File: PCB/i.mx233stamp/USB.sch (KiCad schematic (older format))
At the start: 21 parts, among them U4 GL850G, X2 12MHz

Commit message: conectando mas senales
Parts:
- L7: footprint (none) -> SM0805
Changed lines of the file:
@@
-EESchema Schematic File Version 2  date Fri 05 Aug 2011 02:31:32 PM COT
+EESchema Schematic File Version 2  date Sat 06 Aug 2011 12:43:52 PM COT
 LIBS:con-jack
 LIBS:adm3101e
@@
 Sheet 2 4
 Title ""
-Date "5 aug 2011"
+Date "6 aug 2011"
 Rev ""
 Comp ""
@@
 $EndComp
 $Comp
-L GND #PWR12
+L GND #PWR01
 U 1 1 4E3C4430
 P 10750 3150
-F 0 "#PWR12" H 10750 3150 30  0001 C CNN
+F 0 "#PWR01" H 10750 3150 30  0001 C CNN
 F 1 "GND" H 10750 3080 30  0001 C CNN
 	1    10750 3150
@@
 $EndComp
 $Comp
-L VDD5V #PWR11
+L VDD5V #PWR02
 U 1 1 4E3C4429
 P 10750 2550
-F 0 "#PWR11" H 10750 2650 30  0001 C CNN
+F 0 "#PWR02" H 10750 2650 30  0001 C CNN
 F 1 "VDD5V" H 10750 2650 30  0000 C CNN
 	1    10750 2550
@@
 $EndComp
 $Comp
-L VDD5V #PWR7
+L VDD5V #PWR03
 U 1 1 4E3C4418
 P 9600 2550
-F 0 "#PWR7" H 9600 2650 30  0001 C CNN
+F 0 "#PWR03" H 9600 2650 30  0001 C CNN
 F 1 "VDD5V" H 9600 2650 30  0000 C CNN
 	1    9600 2550
@@
 $EndComp
 $Comp
-L GND #PWR5
+L GND #PWR04
 U 1 1 4E3C436B
 P 8500 1650
-F 0 "#PWR5" H 8500 1650 30  0001 C CNN
+F 0 "#PWR04" H 8500 1650 30  0001 C CNN
 F 1 "GND" H 8500 1580 30  0001 C CNN
 	1    8500 1650
@@
 USBH_P33V
 $Comp
-L VDD5V #PWR8
+L VDD5V #PWR05
 U 1 1 4E3C4207
 P 9600 2950
-F 0 "#PWR8" H 9600 3050 30  0001 C CNN
+F 0 "#PWR05" H 9600 3050 30  0001 C CNN
 F 1 "VDD5V" H 9600 3050 30  0000 C CNN
 	1    9600 2950
@@
 USBH_P33V
 $Comp
-L GND #PWR9
+L GND #PWR06
 U 1 1 4E3C3A60
 P 9900 5600
-F 0 "#PWR9" H 9900 5600 30  0001 C CNN
+F 0 "#PWR06" H 9900 5600 30  0001 C CNN
 F 1 "GND" H 9900 5530 30  0001 C CNN
 	1    9900 5600
@@
 $EndComp
 $Comp
-L GND #PWR4
+L GND #PWR07
 U 1 1 4E3C3A56
 P 8000 5600
-F 0 "#PWR4" H 8000 5600 30  0001 C CNN
+F 0 "#PWR07" H 8000 5600 30  0001 C CNN
 F 1 "GND" H 8000 5530 30  0001 C CNN
 	1    8000 5600
@@
 F 0 "L7" V 9150 4800 40  0000 C CNN
 F 1 "2A 120 ohm" V 9300 4800 40  0000 C CNN
+F 2 "SM0805" H 9200 4800 60  0001 C CNN
 	1    9200 4800
 	0    1    1    0
@@
 andres.calderon@emqbit.com\n
 $Comp
-L GND #PWR3
+L GND #PWR08
 U 1 1 4E3C3807
 P 7100 4300
-F 0 "#PWR3" H 7100 4300 30  0001 C CNN
+F 0 "#PWR08" H 7100 4300 30  0001 C CNN
 F 1 "GND" H 7100 4230 30  0001 C CNN
 	1    7100 4300
@@
 $EndComp
 $Comp
-L GND #PWR10
+L GND #PWR09
 U 1 1 4E3C36BE
 P 10400 3600
-F 0 "#PWR10" H 10400 3600 30  0001 C CNN
+F 0 "#PWR09" H 10400 3600 30  0001 C CNN
 F 1 "GND" H 10400 3530 30  0001 C CNN
 	1    10400 3600
@@
 X1
 $Comp
-L GND #PWR6
+L GND #PWR010
 U 1 1 4E3C222B
 P 9500 3750
-F 0 "#PWR6" H 9500 3750 30  0001 C CNN
+F 0 "#PWR010" H 9500 3750 30  0001 C CNN
 F 1 "GND" H 9500 3680 30  0001 C CNN
 	1    9500 3750
@@
 USB_DM2
 $Comp
-L GND #PWR1
+L GND #PWR011
 U 1 1 4E3C212B
 P 5250 5150
-F 0 "#PWR1" H 5250 5150 30  0001 C CNN
+F 0 "#PWR011" H 5250 5150 30  0001 C CNN
 F 1 "GND" H 5250 5080 30  0001 C CNN
 	1    5250 5150
@@
 $EndComp
 $Comp
-L GND #PWR2
+L GND #PWR012
 U 1 1 4E3C206C
 P 5850 5150
-F 0 "#PWR2" H 5850 5150 30  0001 C CNN
+F 0 "#PWR012" H 5850 5150 30  0001 C CNN
 F 1 "GND" H 5850 5080 30  0001 C CNN
 	1    5850 5150

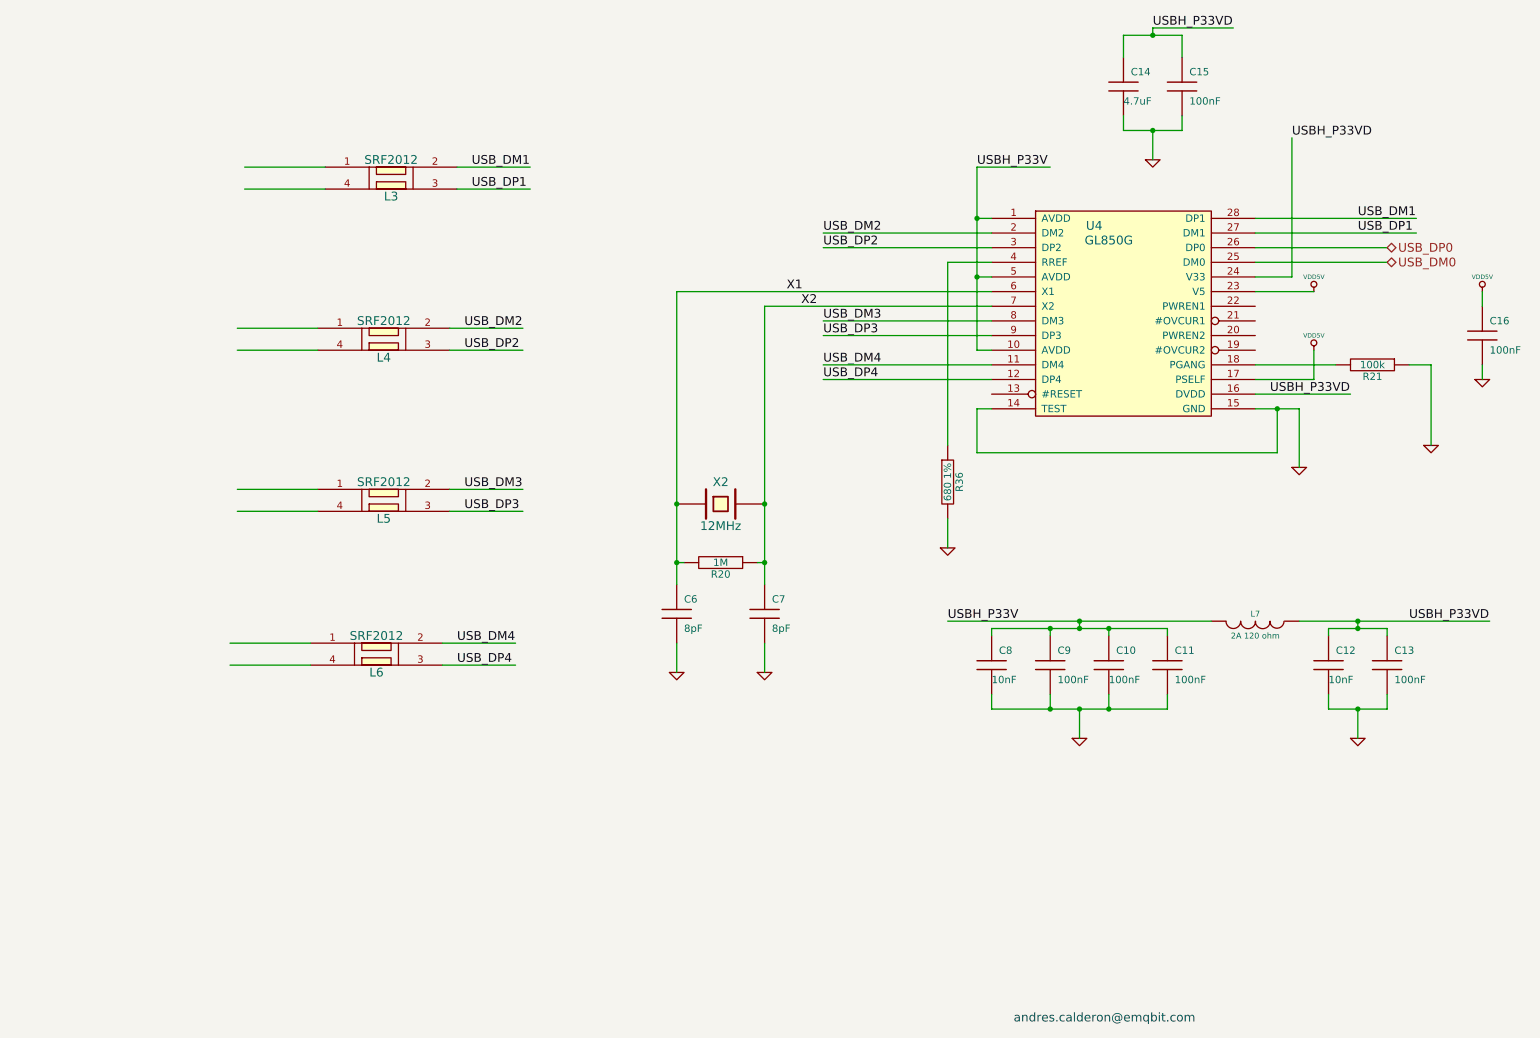
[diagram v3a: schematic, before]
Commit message: Cambios en los footprints, adición de conectores USB host, organización de señales en los conectores
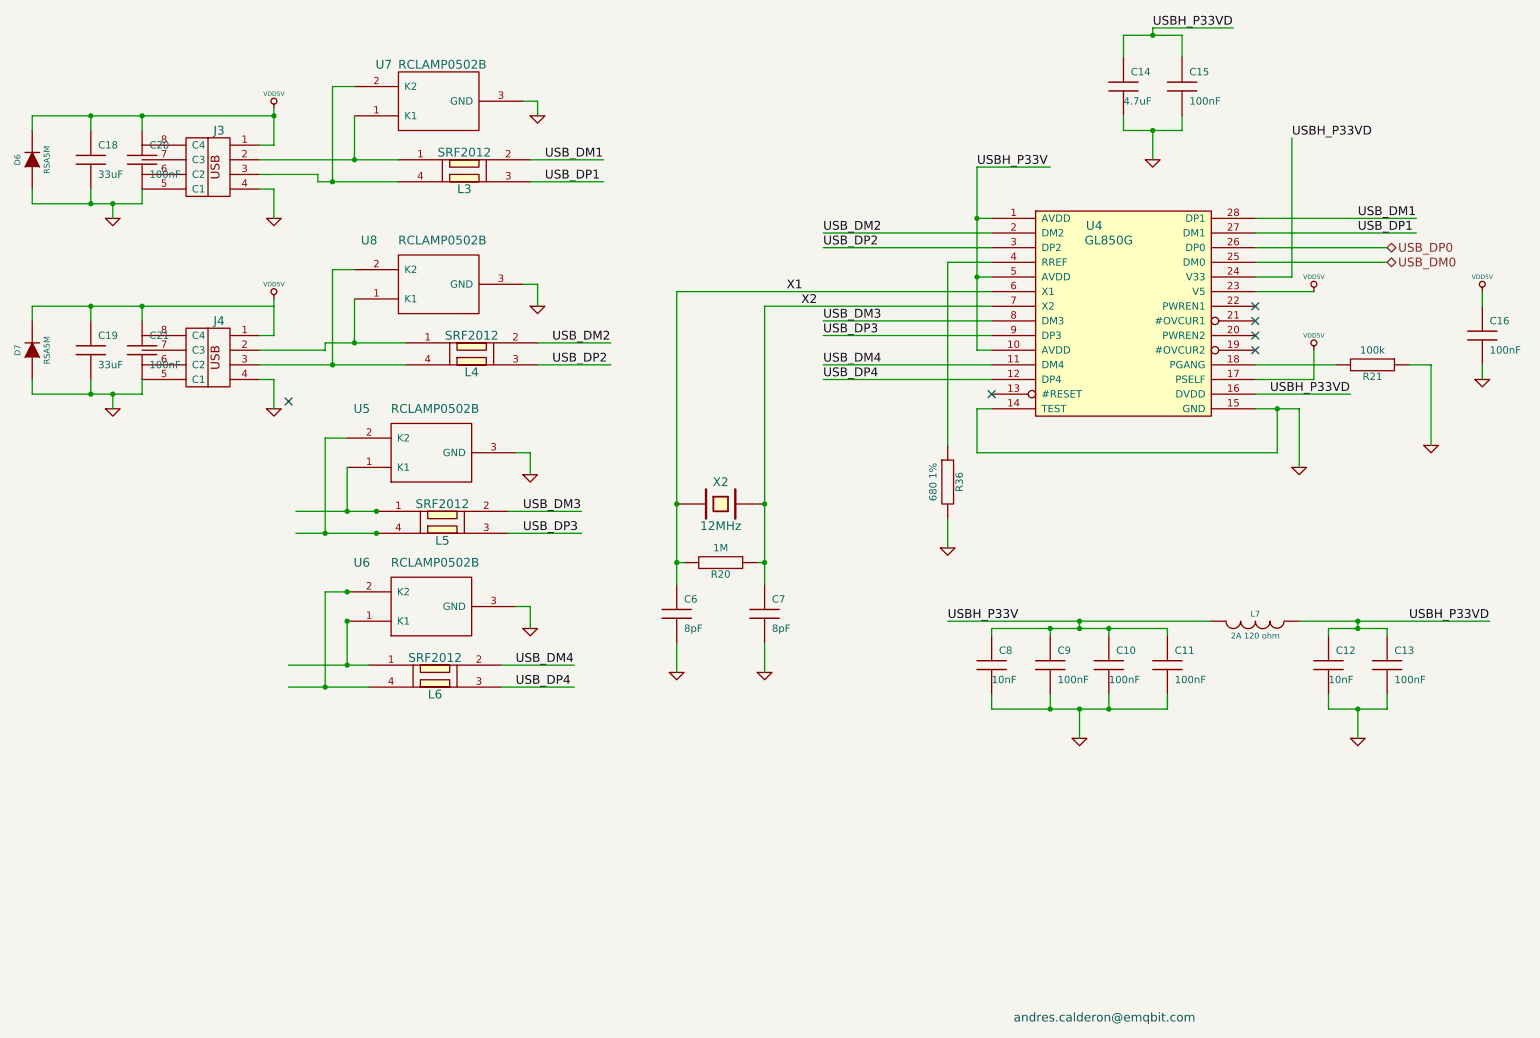
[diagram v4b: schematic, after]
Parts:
- added C18, C19: 33uF, SM1206, symbol C
- added C20, C21: 100nF, SM0603, symbol C
- added D6, D7: RSA5M, diode-1-SOD123, symbol DIODE
- added J3, J4: USB_2, conn_usb_A-vert, symbol USB_2
- added U5, U6, U7, U8: RCLAMP0502B, SOD523, symbol RCLAMP0502B
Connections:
- wire segments 90 -> 140
- no-connect marks 0 -> 6
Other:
- moved on the sheet: L3, L4, L5, L6

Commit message: Adición de conectores USB host, conexión de HP_GND a un conector externo, Cambio de los footprints dela DDR memoria SPI, Q1,
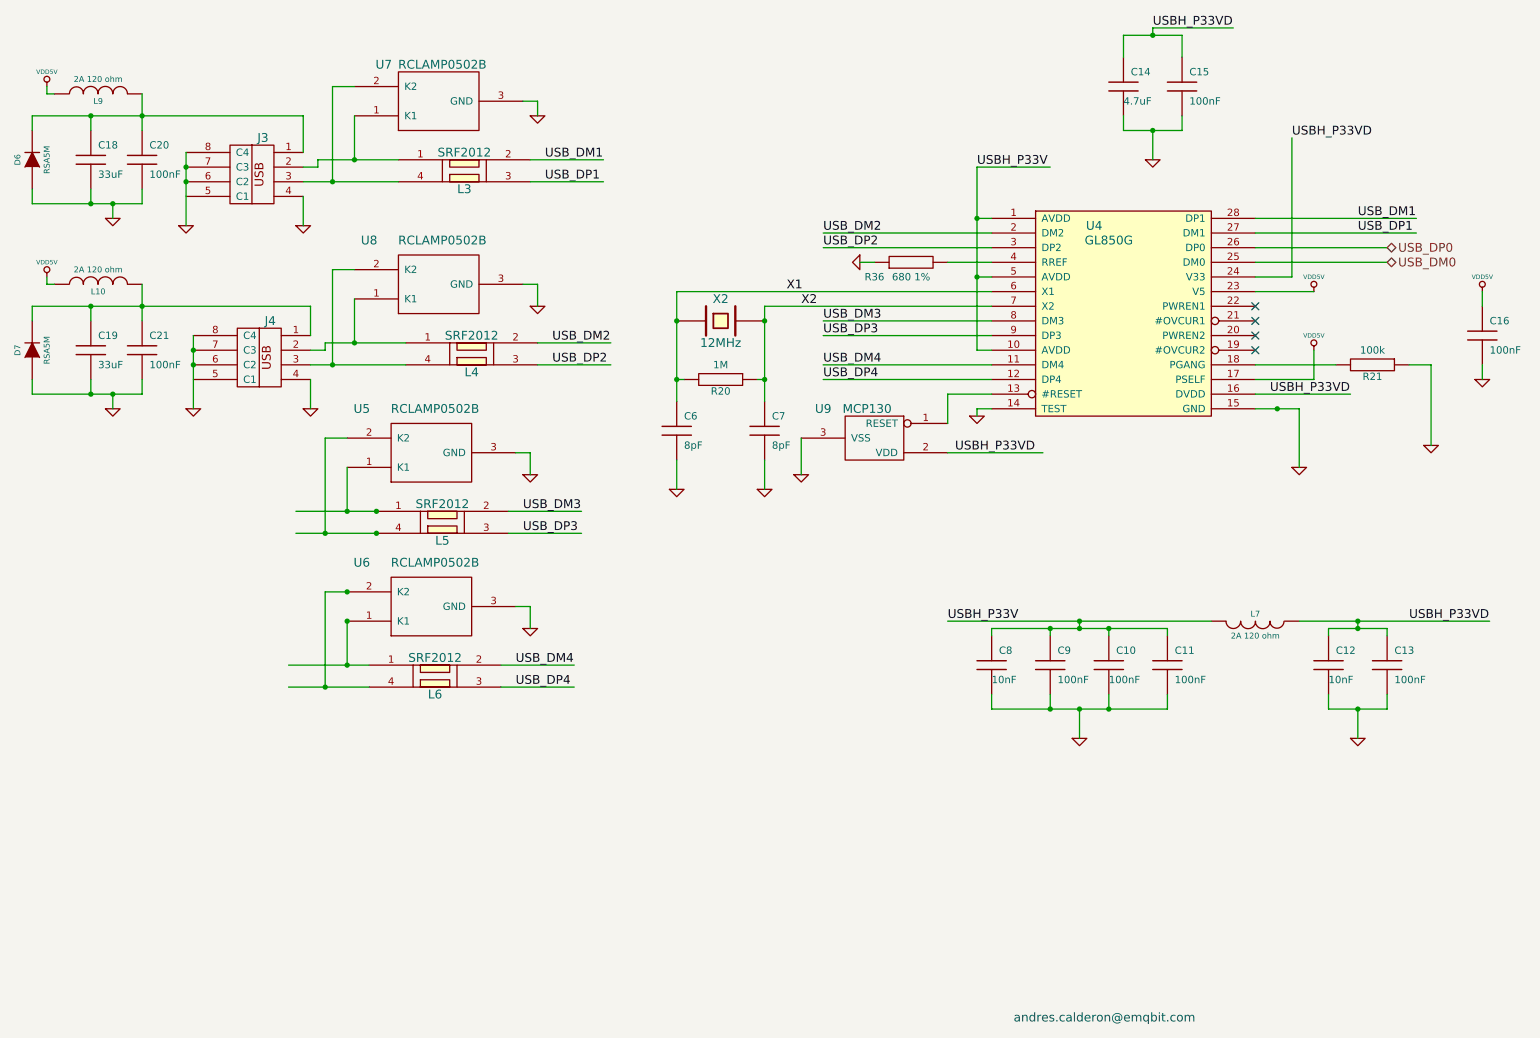
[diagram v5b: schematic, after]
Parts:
- added L10, L9: 2A 120 ohm, SM0805, symbol INDUCTOR
- added U9: MCP130, SOT23B-3, symbol MCP130
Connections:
- wire segments 140 -> 143
- no-connect marks 6 -> 4
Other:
- moved on the sheet: C6, C7, J3, R20, R36, X2
